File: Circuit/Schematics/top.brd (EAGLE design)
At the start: 38.1 x 38.1 mm, 36 parts, among them Y1 16 MHz, Y2 32.768 kHz

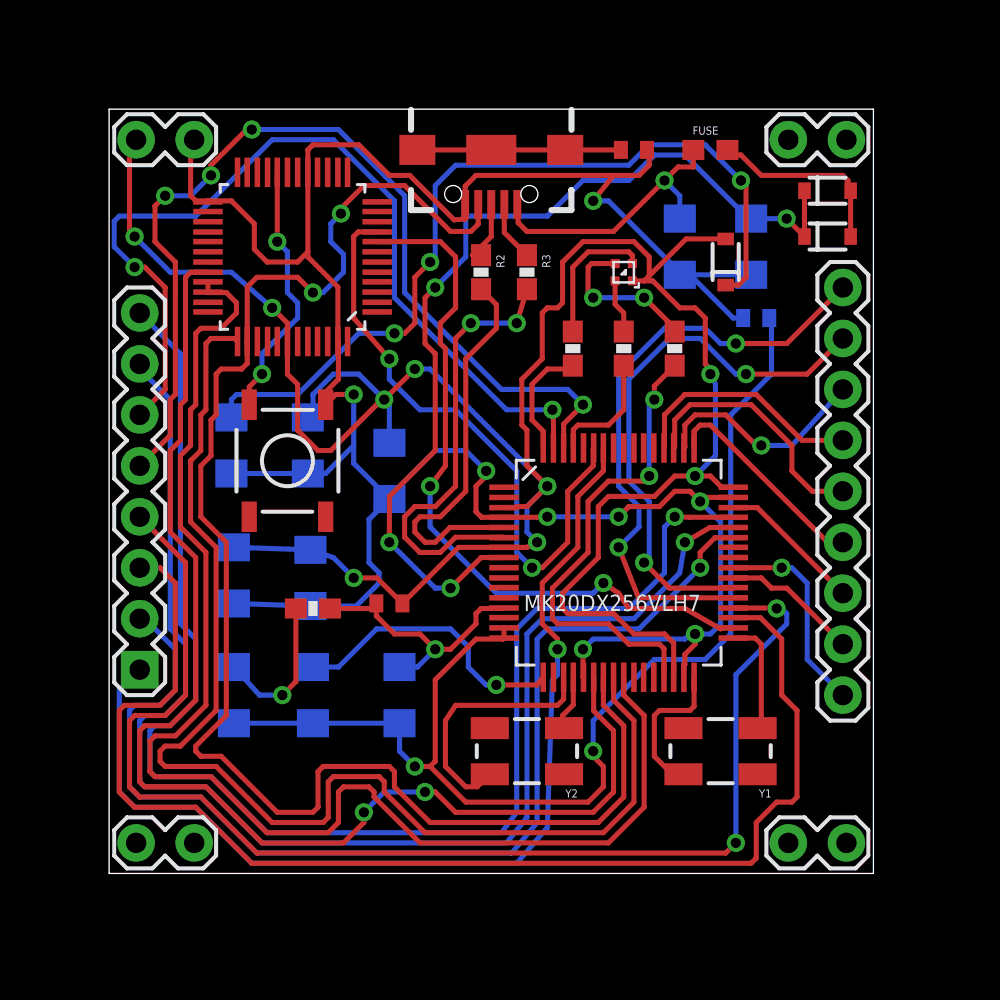
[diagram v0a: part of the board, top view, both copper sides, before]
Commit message: P1 preliminary boards finished
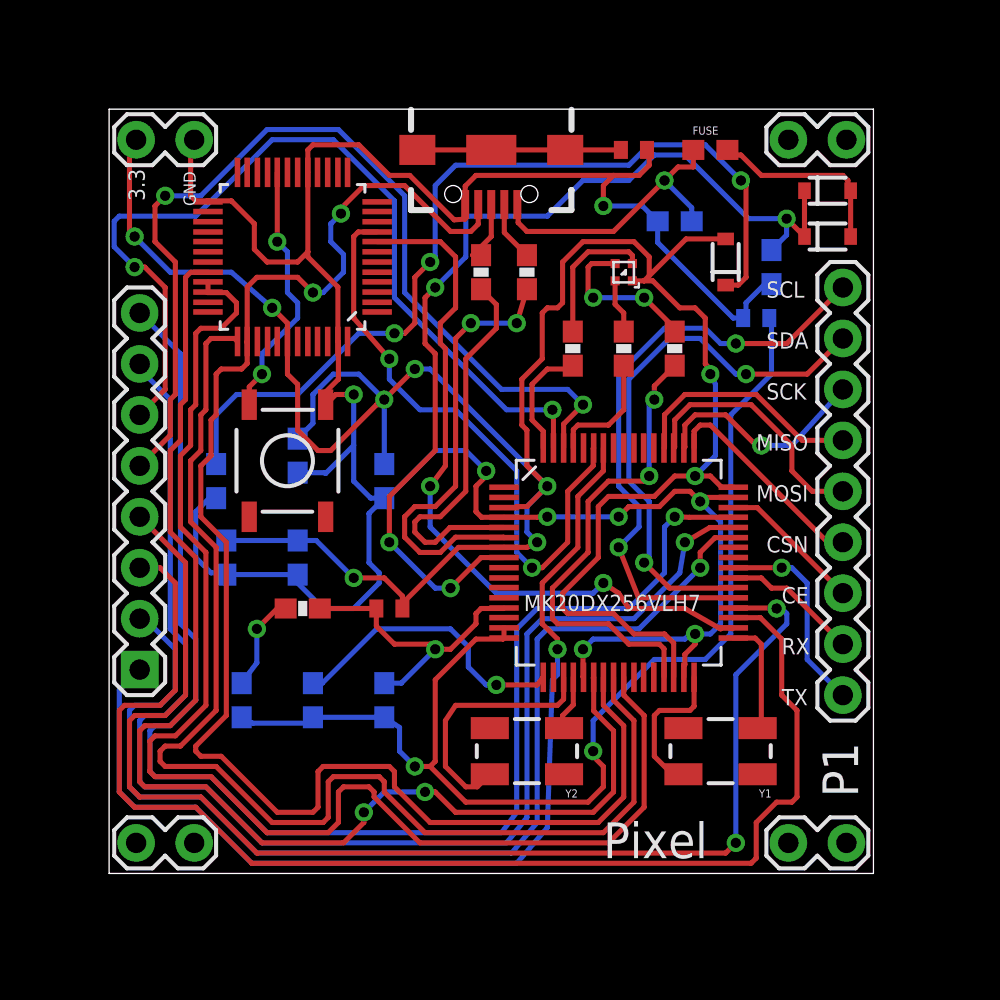
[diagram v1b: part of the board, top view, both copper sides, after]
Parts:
- removed C1, C4, C5, C7, C8, C9: 0.1uF, SparkFun-Capacitors:EIA3216
- removed C10: 2.2uF, SparkFun-Capacitors:EIA3216
- removed C2, C3, C6: 0.1 uF, SparkFun-Capacitors:EIA3216
- added C11, C12, C13, C14, C15, C17, C18, C19, C20: .1 uF, SparkFun-Passives:0603-CAP
- added C16: 2.2 uF, SparkFun-Passives:0603-CAP
- moved R1 0.51 mm to (9.65, 13.2)
- moved FERRITE1 0.25 mm to (14.0, 13.2)
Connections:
- net 3.3V: now also C13.1, C14.1, C15.1, C16.1; no longer C10.A, C7.A, C8.A, C9.A
- net AGND: now also C17.2, C18.2, C19.2; no longer C4.C, C5.C, C6.C
- net GND-ISO: now also C11.1, C12.1, C13.2, C14.2, C15.2, C16.2, C20.2; no longer C1.C, C10.C, C2.C, C3.C, C7.C, C8.C, C9.C
- net N$1: now also C19.1; no longer C4.A
- net N$2: now also C12.2; no longer C1.A
- net N$4: now also C17.1; no longer C6.A
- net N$5: now also C18.1; no longer C5.A
- net N$63: now also C11.2; no longer C3.A
- net N$9: now also C20.1; no longer C2.A
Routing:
- net 3.3V: track 126.5 -> 130.2 mm
- net N$5: track 7.63 -> 4.82 mm
- net N$9: track 41.8 -> 44.5 mm
- net GND-ISO: track 128.7 -> 131.0 mm
- net N$4: track 13.4 -> 15.3 mm
- net N$2: track 47.9 -> 49.8 mm
- net AGND: track 59.2 -> 58.7 mm
- net N$37: track 48.4 -> 48.1 mm, vias 4 -> 2
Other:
- board text added: "1"
- board text added: "2"
- board text added: "3"
- board text added: "3.3"
- board text added: "4"
- board text added: "5"
- board text added: "6"
- board text added: "7"
- board text added: "8"
- board text added: "CE"
- board text added: "CSN"
- board text added: "GND"
- board text added: "MISO"
- board text added: "MOSI"
- board text added: "P1"
- board text added: "Pixel"
- board text added: "RX"
- board text added: "SCK"
- board text added: "SCL"
- board text added: "SDA"
- board text added: "TX"
